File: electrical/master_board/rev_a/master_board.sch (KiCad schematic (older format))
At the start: 4 parts

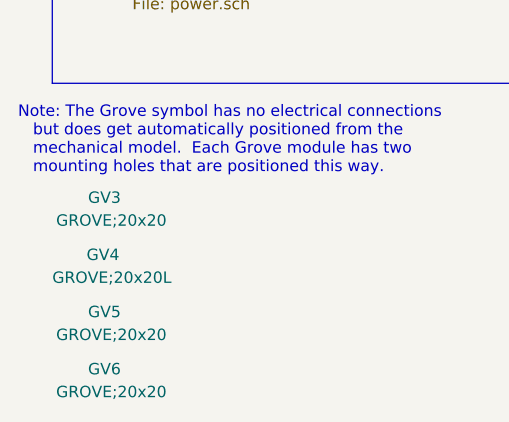
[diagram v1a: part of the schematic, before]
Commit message: Reannoted. Postioned components are in the 80-99 reference range.
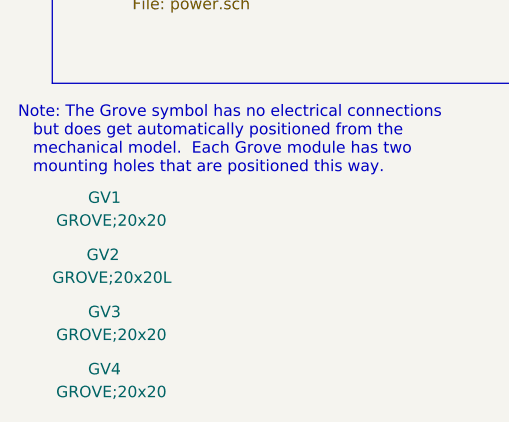
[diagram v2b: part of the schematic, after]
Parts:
- renumbered GV3 to GV1, GV4 to GV2, GV5 to GV3, GV6 to GV4
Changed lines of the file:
@@
 $EndDescr
 $Comp
-L HR2:GROVE;20x20 GV5
+L HR2:GROVE;20x20 GV3
 U 1 1 5F304369
 P 1550 7550
-F 0 "GV5" H 1500 7600 50  0000 L CNN
+F 0 "GV3" H 1500 7600 50  0000 L CNN
 F 1 "GROVE;20x20" H 1300 7500 50  0000 L CNN
 F 2 "HR2:GROVE20x20" H 1750 7600 60  0001 L CNN
@@
 $EndComp
 $Comp
-L HR2:GROVE;20x20 GV6
+L HR2:GROVE;20x20 GV4
 U 1 1 5F304374
 P 1550 7800
-F 0 "GV6" H 1500 7850 50  0000 L CNN
+F 0 "GV4" H 1500 7850 50  0000 L CNN
 F 1 "GROVE;20x20" H 1300 7750 50  0000 L CNN
 F 2 "HR2:GROVE20x20" H 1750 7850 60  0001 L CNN
@@
 Note: The Grove symbol has no electrical connections\n   but does get automatically positioned from the\n   mechanical model.  Each Grove module has two\n   mounting holes that are positioned this way.
 $Comp
-L HR2:GROVE;20x20L GV4
+L HR2:GROVE;20x20L GV2
 U 1 1 5F30889D
 P 1550 7300
-F 0 "GV4" H 1450 7350 50  0000 L CNN
+F 0 "GV2" H 1450 7350 50  0000 L CNN
 F 1 "GROVE;20x20L" H 1300 7250 50  0000 L CNN
 F 2 "HR2:GROVE20x20L" H 1750 7350 60  0001 L CNN
@@
 $EndComp
 $Comp
-L HR2:GROVE;20x20 GV3
+L HR2:GROVE;20x20 GV1
 U 1 1 5F308FA7
 P 1550 7050
-F 0 "GV3" H 1500 7100 50  0000 L CNN
+F 0 "GV1" H 1500 7100 50  0000 L CNN
 F 1 "GROVE;20x20" H 1300 7000 50  0000 L CNN
 F 2 "HR2:GROVE20x20" H 1750 7100 60  0001 L CNN

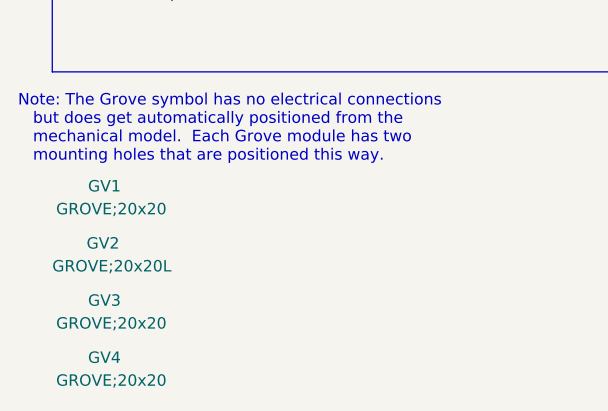
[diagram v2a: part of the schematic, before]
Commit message: Postioned all the components properly.
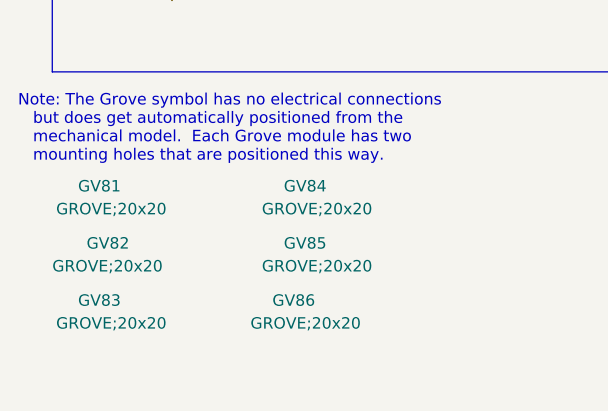
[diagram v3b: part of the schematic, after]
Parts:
- added GV85, GV86: GROVE;20x20, HR2:GROVE20x20, symbol HR2:GROVE;20x20
- GV82: renamed from GV2; value GROVE;20x20L -> GROVE;20x20; footprint HR2:GROVE20x20L -> HR2:GROVE20x20
- renumbered GV1 to GV81, GV3 to GV83, GV4 to GV84
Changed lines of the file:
@@
 $EndDescr
 $Comp
-L HR2:GROVE;20x20 GV3
+L HR2:GROVE;20x20 GV83
 U 1 1 5F304369
 P 1550 7550
-F 0 "GV3" H 1500 7600 50  0000 L CNN
+F 0 "GV83" H 1500 7600 50  0000 L CNN
 F 1 "GROVE;20x20" H 1300 7500 50  0000 L CNN
 F 2 "HR2:GROVE20x20" H 1750 7600 60  0001 L CNN
@@
 $EndComp
 $Comp
-L HR2:GROVE;20x20 GV4
+L HR2:GROVE;20x20 GV84
 U 1 1 5F304374
-P 1550 7800
-F 0 "GV4" H 1500 7850 50  0000 L CNN
-F 1 "GROVE;20x20" H 1300 7750 50  0000 L CNN
-F 2 "HR2:GROVE20x20" H 1750 7850 60  0001 L CNN
-F 3 "Grove 20x20 Module" H 1750 7650 60  0001 L CNN
-F 4 "Grove 20x20 Module" H 1750 7750 60  0001 L CNN "manf#"
-	1    1550 7800
+P 2450 7050
+F 0 "GV84" H 2400 7100 50  0000 L CNN
+F 1 "GROVE;20x20" H 2200 7000 50  0000 L CNN
+F 2 "HR2:GROVE20x20" H 2650 7100 60  0001 L CNN
+F 3 "Grove 20x20 Module" H 2650 6900 60  0001 L CNN
+F 4 "Grove 20x20 Module" H 2650 7000 60  0001 L CNN "manf#"
+	1    2450 7050
 	-1   0    0    -1
 $EndComp
@@
 Note: The Grove symbol has no electrical connections\n   but does get automatically positioned from the\n   mechanical model.  Each Grove module has two\n   mounting holes that are positioned this way.
 $Comp
-L HR2:GROVE;20x20L GV2
+L HR2:GROVE;20x20L GV82
 U 1 1 5F30889D
 P 1550 7300
-F 0 "GV2" H 1450 7350 50  0000 L CNN
-F 1 "GROVE;20x20L" H 1300 7250 50  0000 L CNN
-F 2 "HR2:GROVE20x20L" H 1750 7350 60  0001 L CNN
+F 0 "GV82" H 1450 7350 50  0000 L CNN
+F 1 "GROVE;20x20" H 1300 7250 50  0000 L CNN
+F 2 "HR2:GROVE20x20" H 1750 7350 60  0001 L CNN
 F 3 "Grove 20x20 Module" H 1750 7150 60  0001 L CNN
 F 4 "Grove 20x20 Module" H 1750 7250 60  0001 L CNN "manf#"
@@
 $EndComp
 $Comp
-L HR2:GROVE;20x20 GV1
+L HR2:GROVE;20x20 GV81
 U 1 1 5F308FA7
 P 1550 7050
-F 0 "GV1" H 1500 7100 50  0000 L CNN
+F 0 "GV81" H 1500 7100 50  0000 L CNN
 F 1 "GROVE;20x20" H 1300 7000 50  0000 L CNN
 F 2 "HR2:GROVE20x20" H 1750 7100 60  0001 L CNN
@@
 F13 "WOW_EN" I R 2550 4800 50
 $EndSheet
+$Comp
+L HR2:GROVE;20x20 GV85
+U 1 1 5F97A1E9
+P 2450 7300
+F 0 "GV85" H 2400 7350 50  0000 L CNN
+F 1 "GROVE;20x20" H 2200 7250 50  0000 L CNN
+F 2 "HR2:GROVE20x20" H 2650 7350 60  0001 L CNN
+F 3 "Grove 20x20 Module" H 2650 7150 60  0001 L CNN
+F 4 "Grove 20x20 Module" H 2650 7250 60  0001 L CNN "manf#"
+	1    2450 7300
+	-1   0    0    -1
+$EndComp
+$Comp
+L HR2:GROVE;20x20 GV86
+U 1 1 5F98D40B
+P 2400 7550
+F 0 "GV86" H 2350 7600 50  0000 L CNN
+F 1 "GROVE;20x20" H 2150 7500 50  0000 L CNN
+F 2 "HR2:GROVE20x20" H 2600 7600 60  0001 L CNN
+F 3 "Grove 20x20 Module" H 2600 7400 60  0001 L CNN
+F 4 "Grove 20x20 Module" H 2600 7500 60  0001 L CNN "manf#"
+	1    2400 7550
+	-1   0    0    -1
+$EndComp
 Wire Bus Line
 	7600 3700 7600 4200

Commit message: Got the spacer holes placed onto the PCB.
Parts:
- added H1, H2, H3, H4, H5, H6: HOLE;M2.5, MountingHole:MountingHole_2.7mm_M2.5, symbol HR2:HOLE;M2.5
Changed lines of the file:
@@
 	-1   0    0    -1
+$EndComp
+$Comp
+L HR2:HOLE;M2.5 H1
+U 1 1 5F98C15A
+P 3450 6800
+F 0 "H1" H 3475 6846 50  0000 L CNN
+F 1 "HOLE;M2.5" H 3475 6755 50  0000 L CNN
+F 2 "MountingHole:MountingHole_2.7mm_M2.5" H 3650 6850 60  0001 L CNN
+F 3 "M2.5 Mounting Hole" H 3650 6650 60  0001 L CNN
+F 4 "M2.5 Mounting Hole" H 3650 6750 60  0001 L CNN "manf#"
+	1    3450 6800
+	1    0    0    -1
+$EndComp
+$Comp
+L HR2:HOLE;M2.5 H2
+U 1 1 5F98CA97
+P 3450 7000
+F 0 "H2" H 3475 7046 50  0000 L CNN
+F 1 "HOLE;M2.5" H 3475 6955 50  0000 L CNN
+F 2 "MountingHole:MountingHole_2.7mm_M2.5" H 3650 7050 60  0001 L CNN
+F 3 "M2.5 Mounting Hole" H 3650 6850 60  0001 L CNN
+F 4 "M2.5 Mounting Hole" H 3650 6950 60  0001 L CNN "manf#"
+	1    3450 7000
+	1    0    0    -1
+$EndComp
+$Comp
+L HR2:HOLE;M2.5 H3
+U 1 1 5F99FB35
+P 3450 7200
+F 0 "H3" H 3475 7246 50  0000 L CNN
+F 1 "HOLE;M2.5" H 3475 7155 50  0000 L CNN
+F 2 "MountingHole:MountingHole_2.7mm_M2.5" H 3650 7250 60  0001 L CNN
+F 3 "M2.5 Mounting Hole" H 3650 7050 60  0001 L CNN
+F 4 "M2.5 Mounting Hole" H 3650 7150 60  0001 L CNN "manf#"
+	1    3450 7200
+	1    0    0    -1
+$EndComp
+$Comp
+L HR2:HOLE;M2.5 H4
+U 1 1 5F99FB96
+P 3900 6800
+F 0 "H4" H 3925 6846 50  0000 L CNN
+F 1 "HOLE;M2.5" H 3925 6755 50  0000 L CNN
+F 2 "MountingHole:MountingHole_2.7mm_M2.5" H 4100 6850 60  0001 L CNN
+F 3 "M2.5 Mounting Hole" H 4100 6650 60  0001 L CNN
+F 4 "M2.5 Mounting Hole" H 4100 6750 60  0001 L CNN "manf#"
+	1    3900 6800
+	1    0    0    -1
+$EndComp
+$Comp
+L HR2:HOLE;M2.5 H5
+U 1 1 5F9B303C
+P 3900 7000
+F 0 "H5" H 3925 7046 50  0000 L CNN
+F 1 "HOLE;M2.5" H 3925 6955 50  0000 L CNN
+F 2 "MountingHole:MountingHole_2.7mm_M2.5" H 4100 7050 60  0001 L CNN
+F 3 "M2.5 Mounting Hole" H 4100 6850 60  0001 L CNN
+F 4 "M2.5 Mounting Hole" H 4100 6950 60  0001 L CNN "manf#"
+	1    3900 7000
+	1    0    0    -1
+$EndComp
+$Comp
+L HR2:HOLE;M2.5 H6
+U 1 1 5F9B30B1
+P 3900 7200
+F 0 "H6" H 3925 7246 50  0000 L CNN
+F 1 "HOLE;M2.5" H 3925 7155 50  0000 L CNN
+F 2 "MountingHole:MountingHole_2.7mm_M2.5" H 4100 7250 60  0001 L CNN
+F 3 "M2.5 Mounting Hole" H 4100 7050 60  0001 L CNN
+F 4 "M2.5 Mounting Hole" H 4100 7150 60  0001 L CNN "manf#"
+	1    3900 7200
+	1    0    0    -1
 $EndComp
 Wire Bus Line

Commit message: Changing footprints and moving things around on the PCB.
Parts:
- removed GV84: GROVE;20x20, HR2:GROVE20x20, symbol HR2:GROVE;20x20
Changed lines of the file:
@@
-	-1   0    0    -1
-$EndComp
-$Comp
-L HR2:GROVE;20x20 GV84
-U 1 1 5F304374
-P 2450 7050
-F 0 "GV84" H 2400 7100 50  0000 L CNN
-F 1 "GROVE;20x20" H 2200 7000 50  0000 L CNN
-F 2 "HR2:GROVE20x20" H 2650 7100 60  0001 L CNN
-F 3 "Grove 20x20 Module" H 2650 6900 60  0001 L CNN
-F 4 "Grove 20x20 Module" H 2650 7000 60  0001 L CNN "manf#"
-	1    2450 7050
 	-1   0    0    -1
 $EndComp
@@
 L HR2:GROVE;20x20 GV85
 U 1 1 5F97A1E9
-P 2450 7300
-F 0 "GV85" H 2400 7350 50  0000 L CNN
-F 1 "GROVE;20x20" H 2200 7250 50  0000 L CNN
-F 2 "HR2:GROVE20x20" H 2650 7350 60  0001 L CNN
-F 3 "Grove 20x20 Module" H 2650 7150 60  0001 L CNN
-F 4 "Grove 20x20 Module" H 2650 7250 60  0001 L CNN "manf#"
-	1    2450 7300
+P 2400 7050
+F 0 "GV85" H 2350 7100 50  0000 L CNN
+F 1 "GROVE;20x20" H 2150 7000 50  0000 L CNN
+F 2 "HR2:GROVE20x20" H 2600 7100 60  0001 L CNN
+F 3 "Grove 20x20 Module" H 2600 6900 60  0001 L CNN
+F 4 "Grove 20x20 Module" H 2600 7000 60  0001 L CNN "manf#"
+	1    2400 7050
 	-1   0    0    -1
 $EndComp
@@
 L HR2:GROVE;20x20 GV86
 U 1 1 5F98D40B
-P 2400 7550
-F 0 "GV86" H 2350 7600 50  0000 L CNN
-F 1 "GROVE;20x20" H 2150 7500 50  0000 L CNN
-F 2 "HR2:GROVE20x20" H 2600 7600 60  0001 L CNN
-F 3 "Grove 20x20 Module" H 2600 7400 60  0001 L CNN
-F 4 "Grove 20x20 Module" H 2600 7500 60  0001 L CNN "manf#"
-	1    2400 7550
+P 2400 7300
+F 0 "GV86" H 2350 7350 50  0000 L CNN
+F 1 "GROVE;20x20" H 2150 7250 50  0000 L CNN
+F 2 "HR2:GROVE20x20" H 2600 7350 60  0001 L CNN
+F 3 "Grove 20x20 Module" H 2600 7150 60  0001 L CNN
+F 4 "Grove 20x20 Module" H 2600 7250 60  0001 L CNN "manf#"
+	1    2400 7300
 	-1   0    0    -1
 $EndComp

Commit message: More work thinning rats nest of unconnected wires.
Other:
- note added: "TO DO:\n1. Make sure all off the standoff holes have no trace incursion.\n2. Work on Ground bottleneck.\n3. Ground stitch."
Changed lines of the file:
@@
 	1    0    0    -1
 $EndComp
+Text Notes 2050 7950 0    80   ~ 0
+TO DO:\n1. Make sure all off the standoff holes have no trace incursion.\n2. Work on Ground bottleneck.\n3. Ground stitch.
 Wire Bus Line
 	7600 3700 7600 4200

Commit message: More work on ground planes.
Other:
- note added: "TO DO:\n1. Work on Ground bottleneck.\n2. Ground stitch."
- note removed: "TO DO:\n1. Make sure all off the standoff holes have no trace incursion.\n2. Work on Ground bottleneck.\n3. Ground stitch."
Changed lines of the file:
@@
 $EndComp
 Text Notes 2050 7950 0    80   ~ 0
-TO DO:\n1. Make sure all off the standoff holes have no trace incursion.\n2. Work on Ground bottleneck.\n3. Ground stitch.
+TO DO:\n1. Work on Ground bottleneck.\n2. Ground stitch.
 Wire Bus Line
 	7600 3700 7600 4200

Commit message: Pin reassignments to support servo current.
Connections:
- net labels added: SERVO_CUR, SERVO_POS
- wire segments 154 -> 158
